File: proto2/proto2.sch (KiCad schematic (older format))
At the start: 7 parts, among them SW1 SW_DIP_x04

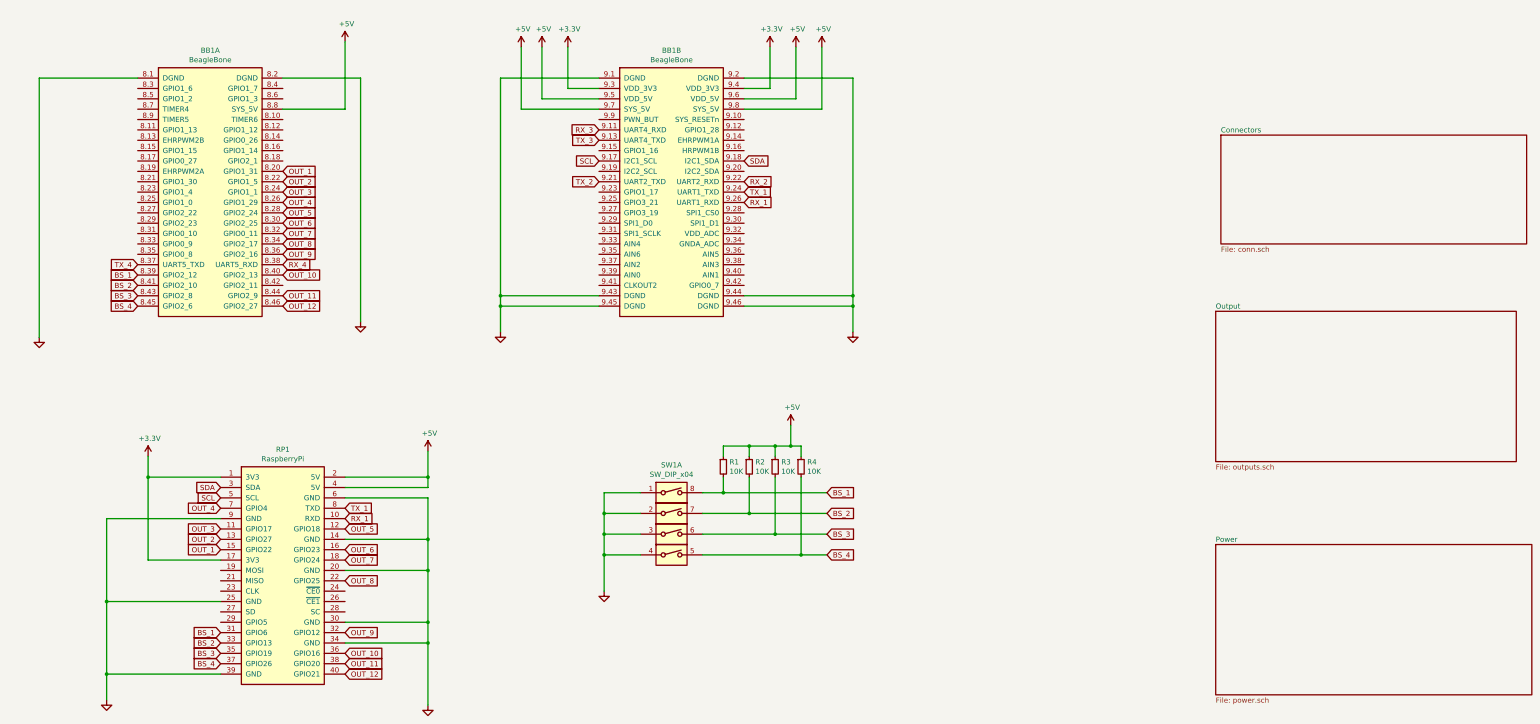
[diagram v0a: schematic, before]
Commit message: Routed Board.
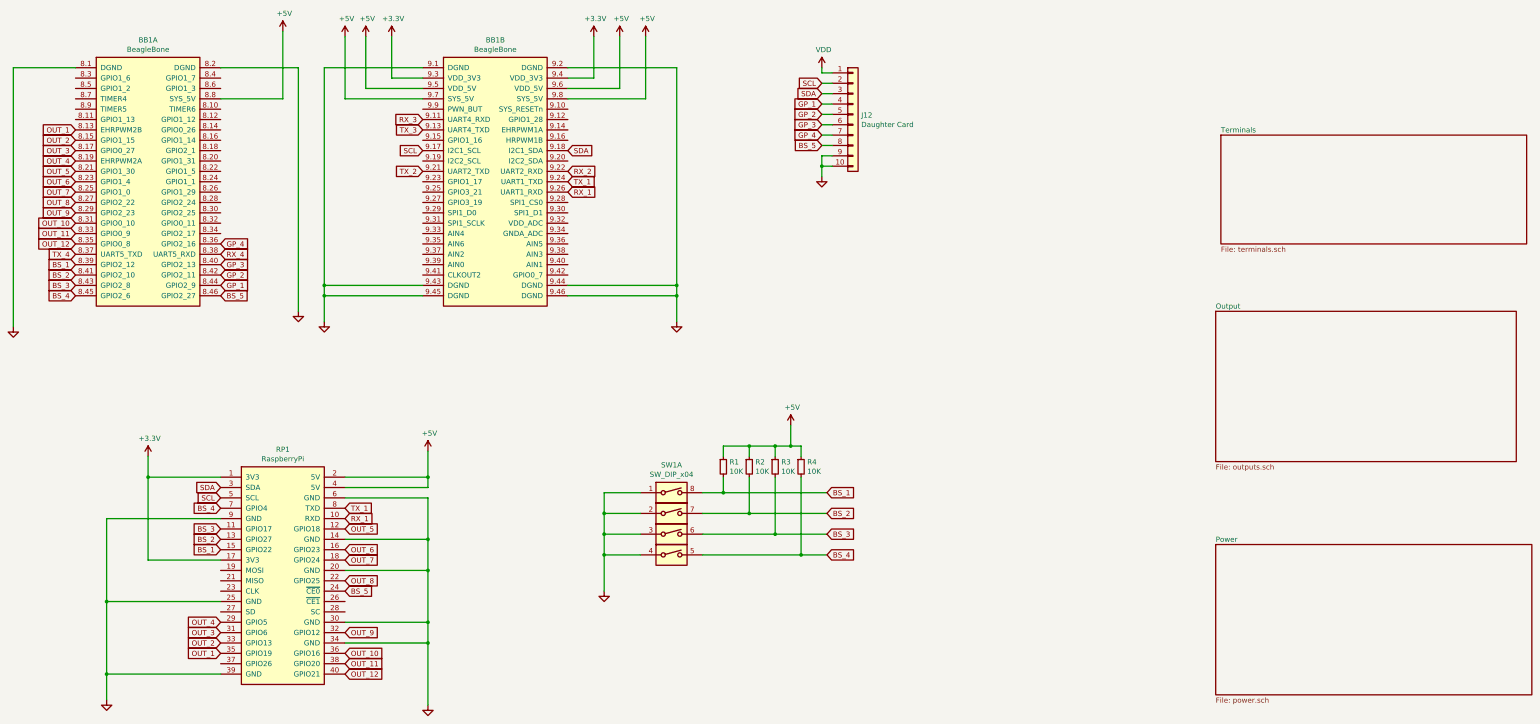
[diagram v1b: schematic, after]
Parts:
- added J12: Daughter Card, Connector_PinHeader_2.54mm:PinHeader_1x10_P2.54mm_Vertical, symbol Connector_Generic:Conn_01x10
- SW1: footprint Package_SO:SOP-8_6.62x9.15mm_P2.54mm -> Button_Switch_BCR:CUI_DS04-254-2-04BK-SMT
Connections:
- net BS_1: now also RP1.15 (GPIO22); no longer RP1.31 (GPIO6)
- net BS_2: now also RP1.13 (GPIO27); no longer RP1.33 (GPIO13)
- net BS_3: now also RP1.11 (GPIO17); no longer RP1.35 (GPIO19)
- net BS_4: now also RP1.7 (GPIO4); no longer RP1.37 (GPIO26)
- net GND: now also J12.10 (Pin_10), J12.9 (Pin_9)
- net OUT_1: now also BB1.8.13 (EHRPWM2B), RP1.35 (GPIO19); no longer BB1.8.20 (GPIO1_31), RP1.15 (GPIO22)
- net OUT_10: now also BB1.8.31 (GPIO0_10); no longer BB1.8.40 (GPIO2_13)
- net OUT_11: now also BB1.8.33 (GPIO0_9); no longer BB1.8.44 (GPIO2_9)
- net OUT_12: now also BB1.8.35 (GPIO0_8); no longer BB1.8.46 (GPIO2_27)
- net OUT_2: now also BB1.8.15 (GPIO1_15), RP1.33 (GPIO13); no longer BB1.8.22 (GPIO1_5), RP1.13 (GPIO27)
- net OUT_3: now also BB1.8.17 (GPIO0_27), RP1.31 (GPIO6); no longer BB1.8.24 (GPIO1_1), RP1.11 (GPIO17)
- net OUT_4: now also BB1.8.19 (EHRPWM2A), RP1.29 (GPIO5); no longer BB1.8.26 (GPIO1_29), RP1.7 (GPIO4)
- net OUT_5: now also BB1.8.21 (GPIO1_30); no longer BB1.8.28 (GPIO2_24)
- net OUT_6: now also BB1.8.23 (GPIO1_4); no longer BB1.8.30 (GPIO2_25)
- net OUT_7: now also BB1.8.25 (GPIO1_0); no longer BB1.8.32 (GPIO0_11)
- net OUT_8: now also BB1.8.27 (GPIO2_22); no longer BB1.8.34 (GPIO2_17)
- net OUT_9: now also BB1.8.29 (GPIO2_23); no longer BB1.8.36 (GPIO2_16)
- net SCL: now also J12.2 (Pin_2)
- net SDA: now also J12.3 (Pin_3)
- net GP_2: now reaches BB1.8.42 (GPIO2_11)
- net GP_2: now also J12.5 (Pin_5)
- net BS_5: now reaches RP1.24 (~CE0~)
- net BS_5: now also BB1.8.46 (GPIO2_27), J12.8 (Pin_8)
- new net GP_1: BB1.8.44 (GPIO2_9), J12.4 (Pin_4)
- new net GP_3: BB1.8.40 (GPIO2_13), J12.6 (Pin_6)
- new net GP_4: BB1.8.36 (GPIO2_16), J12.7 (Pin_7)
- new net VDD: J12.1 (Pin_1)
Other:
- moved on the sheet: BB1A, BB1B

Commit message: Finished routing board and other changes, bad commit message, I know.
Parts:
- R1, R2, R3, R4: LCSC (none) -> C17414
- SW1: LCSC (none) -> C306873; Manufacturer (none) -> Omron; Part Number (none) -> A6S-4101-H
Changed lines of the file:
@@
 F 2 "Button_Switch_BCR:CUI_DS04-254-2-04BK-SMT" H 7300 5400 50  0001 C CNN
 F 3 "~" H 7300 5400 50  0001 C CNN
+F 4 "C306873" H 7300 5400 50  0001 C CNN "LCSC"
+F 5 "Omron" H 7300 5400 50  0001 C CNN "Manufacturer"
+F 6 "A6S-4101-H" H 7300 5400 50  0001 C CNN "Part Number"
 	1    7300 5400
 	1    0    0    -1
@@
 F 2 "Button_Switch_BCR:CUI_DS04-254-2-04BK-SMT" H 7300 5600 50  0001 C CNN
 F 3 "~" H 7300 5600 50  0001 C CNN
+F 4 "C306873" H 7300 5600 50  0001 C CNN "LCSC"
+F 5 "Omron" H 7300 5600 50  0001 C CNN "Manufacturer"
+F 6 "A6S-4101-H" H 7300 5600 50  0001 C CNN "Part Number"
 	2    7300 5600
 	1    0    0    -1
@@
 F 2 "Button_Switch_BCR:CUI_DS04-254-2-04BK-SMT" H 7300 5800 50  0001 C CNN
 F 3 "~" H 7300 5800 50  0001 C CNN
+F 4 "C306873" H 7300 5800 50  0001 C CNN "LCSC"
+F 5 "Omron" H 7300 5800 50  0001 C CNN "Manufacturer"
+F 6 "A6S-4101-H" H 7300 5800 50  0001 C CNN "Part Number"
 	3    7300 5800
 	1    0    0    -1
@@
 F 2 "Button_Switch_BCR:CUI_DS04-254-2-04BK-SMT" H 7300 6000 50  0001 C CNN
 F 3 "~" H 7300 6000 50  0001 C CNN
+F 4 "C306873" H 7300 6000 50  0001 C CNN "LCSC"
+F 5 "Omron" H 7300 6000 50  0001 C CNN "Manufacturer"
+F 6 "A6S-4101-H" H 7300 6000 50  0001 C CNN "Part Number"
 	4    7300 6000
 	1    0    0    -1
@@
 F 2 "Resistor_SMD:R_0805_2012Metric" H 7800 5150 50  0001 C CNN
 F 3 "~" H 7800 5150 50  0001 C CNN
+F 4 "C17414" H 7800 5150 50  0001 C CNN "LCSC"
 	1    7800 5150
 	1    0    0    -1
@@
 F 2 "Resistor_SMD:R_0805_2012Metric" H 8050 5150 50  0001 C CNN
 F 3 "~" H 8050 5150 50  0001 C CNN
+F 4 "C17414" H 8050 5150 50  0001 C CNN "LCSC"
 	1    8050 5150
 	1    0    0    -1
@@
 F 2 "Resistor_SMD:R_0805_2012Metric" H 8300 5150 50  0001 C CNN
 F 3 "~" H 8300 5150 50  0001 C CNN
+F 4 "C17414" H 8300 5150 50  0001 C CNN "LCSC"
 	1    8300 5150
 	1    0    0    -1
@@
 F 2 "Resistor_SMD:R_0805_2012Metric" H 8550 5150 50  0001 C CNN
 F 3 "~" H 8550 5150 50  0001 C CNN
+F 4 "C17414" H 8550 5150 50  0001 C CNN "LCSC"
 	1    8550 5150
 	1    0    0    -1

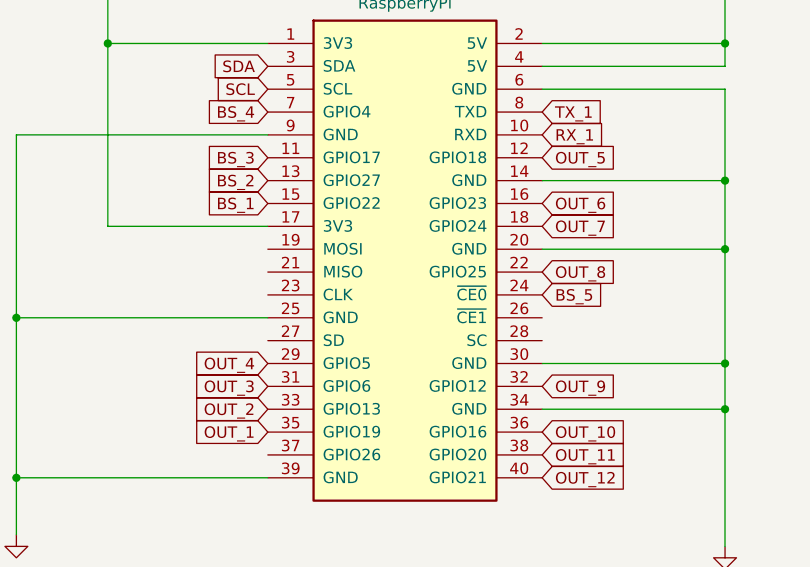
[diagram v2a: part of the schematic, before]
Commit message: Updated drill hole sizes.
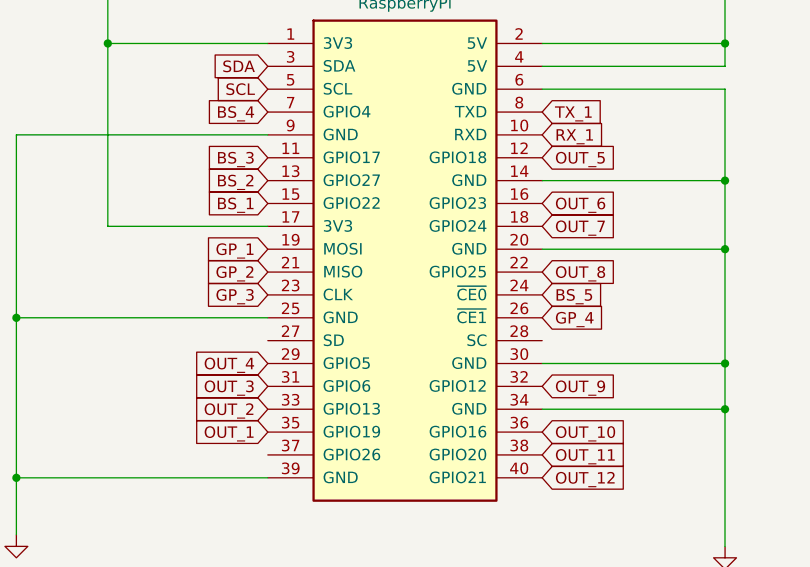
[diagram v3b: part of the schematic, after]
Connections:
- net GP_1: now also RP1.19 (MOSI)
- net GP_2: now also RP1.21 (MISO)
- net GP_3: now also RP1.23 (CLK)
- net GP_4: now also RP1.26 (~CE1~)
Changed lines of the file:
@@
 Text GLabel 2950 3000 2    50   Input ~ 0
 GP_4
+Text GLabel 2950 6250 0    50   Input ~ 0
+GP_2
+Text GLabel 2950 6150 0    50   Input ~ 0
+GP_1
+Text GLabel 2950 6350 0    50   Input ~ 0
+GP_3
+Text GLabel 4150 6450 2    50   Input ~ 0
+GP_4
 $EndSCHEMATC

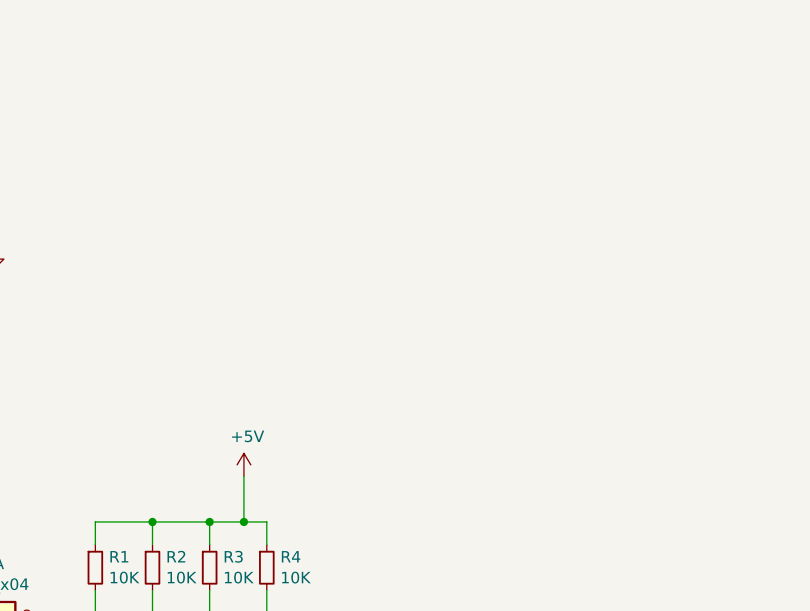
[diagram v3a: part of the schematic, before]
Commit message: Added MOSFET drivers for the SSRs, pullups for I2C, and referenced DIP switches to 3V3.
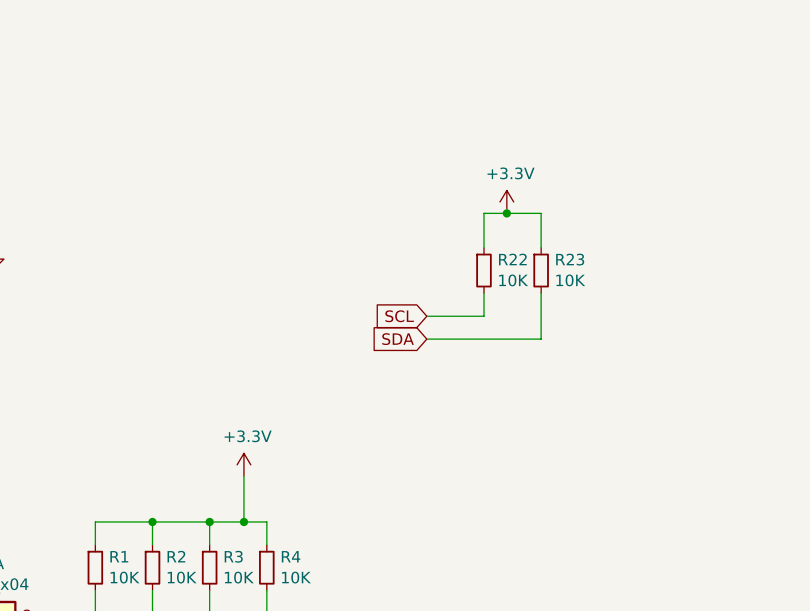
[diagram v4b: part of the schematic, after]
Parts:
- added R22, R23: 10K, Resistor_SMD:R_0805_2012Metric, symbol Device:R_Small
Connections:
- net +3V3: now also R1.1, R2.1, R3.1, R4.1, R22.1, R23.1
- net +5V: no longer R1.1, R2.1, R3.1, R4.1
- net SCL: now also R22.2
- net SDA: now also R23.2
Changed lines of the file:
@@
-	1    0    0    -1
-$EndComp
-$Comp
-L power:+5V #PWR012
-U 1 1 61C71586
-P 8450 4750
-F 0 "#PWR012" H 8450 4600 50  0001 C CNN
-F 1 "+5V" H 8465 4923 50  0000 C CNN
-F 2 "" H 8450 4750 50  0001 C CNN
-F 3 "" H 8450 4750 50  0001 C CNN
-	1    8450 4750
 	1    0    0    -1
 $EndComp
@@
 Text GLabel 4150 6450 2    50   Input ~ 0
 GP_4
+Text GLabel 9250 4050 0    50   Input ~ 0
+SCL
+Text GLabel 9250 4150 0    50   Input ~ 0
+SDA
+$Comp
+L Device:R_Small R22
+U 1 1 61C552C7
+P 9500 3850
+F 0 "R22" H 9559 3896 50  0000 L CNN
+F 1 "10K" H 9559 3805 50  0000 L CNN
+F 2 "Resistor_SMD:R_0805_2012Metric" H 9500 3850 50  0001 C CNN
+F 3 "~" H 9500 3850 50  0001 C CNN
+F 4 "C17414" H 9500 3850 50  0001 C CNN "LCSC"
+	1    9500 3850
+	1    0    0    -1
+$EndComp
+$Comp
+L Device:R_Small R23
+U 1 1 61C5592E
+P 9750 3850
+F 0 "R23" H 9809 3896 50  0000 L CNN
+F 1 "10K" H 9809 3805 50  0000 L CNN
+F 2 "Resistor_SMD:R_0805_2012Metric" H 9750 3850 50  0001 C CNN
+F 3 "~" H 9750 3850 50  0001 C CNN
+F 4 "C17414" H 9750 3850 50  0001 C CNN "LCSC"
+	1    9750 3850
+	1    0    0    -1
+$EndComp
+Wire Wire Line
+	9250 4150 9750 4150
+Wire Wire Line
+	9750 4150 9750 3950
+Wire Wire Line
+	9250 4050 9500 4050
+Wire Wire Line
+	9500 4050 9500 3950
+$Comp
+L power:+3.3V #PWR018
+U 1 1 61C5AD9E
+P 8450 4750
+F 0 "#PWR018" H 8450 4600 50  0001 C CNN
+F 1 "+3.3V" H 8465 4923 50  0000 C CNN
+F 2 "" H 8450 4750 50  0001 C CNN
+F 3 "" H 8450 4750 50  0001 C CNN
+	1    8450 4750
+	1    0    0    -1
+$EndComp
+$Comp
+L power:+3.3V #PWR012
+U 1 1 61C5B4B0
+P 9600 3600
+F 0 "#PWR012" H 9600 3450 50  0001 C CNN
+F 1 "+3.3V" H 9615 3773 50  0000 C CNN
+F 2 "" H 9600 3600 50  0001 C CNN
+F 3 "" H 9600 3600 50  0001 C CNN
+	1    9600 3600
+	1    0    0    -1
+$EndComp
+Wire Wire Line
+	9500 3750 9500 3600
+Wire Wire Line
+	9500 3600 9600 3600
+Wire Wire Line
+	9750 3600 9750 3750
+Connection ~ 9600 3600
+Wire Wire Line
+	9600 3600 9750 3600
 $EndSCHEMATC
